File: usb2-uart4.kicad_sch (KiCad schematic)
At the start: 24 parts, among them U1 CH344Q, U13 TPNUP2202W1T2G, Y1 8MHz

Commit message: switch C28-C33 to 0603
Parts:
- C44, C45, C46, C47, C48, C50: footprint Capacitor_SMD:C_0805_2012Metric_Pad1.18x1.45mm_HandSolder -> Capacitor_SMD:C_0603_1608Metric_Pad1.08x0.95mm_HandSolder
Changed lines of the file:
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@@
       (effects (font (size 1.27 1.27)))
     )
-    (property "Footprint" "Capacitor_SMD:C_0805_2012Metric_Pad1.18x1.45mm_HandSolder" (at 126.365 85.09 0)
+    (property "Footprint" "Capacitor_SMD:C_0603_1608Metric_Pad1.08x0.95mm_HandSolder" (at 126.365 85.09 0)
       (effects (font (size 1.27 1.27)) hide)
     )
@@
       (effects (font (size 1.27 1.27)) (justify right))
     )
-    (property "Footprint" "Capacitor_SMD:C_0805_2012Metric_Pad1.18x1.45mm_HandSolder" (at 144.145 119.38 0)
+    (property "Footprint" "Capacitor_SMD:C_0603_1608Metric_Pad1.08x0.95mm_HandSolder" (at 144.145 119.38 0)
       (effects (font (size 1.27 1.27)) hide)
     )
@@
       (effects (font (size 1.27 1.27)))
     )
-    (property "Footprint" "Capacitor_SMD:C_0805_2012Metric_Pad1.18x1.45mm_HandSolder" (at 126.365 81.28 0)
+    (property "Footprint" "Capacitor_SMD:C_0603_1608Metric_Pad1.08x0.95mm_HandSolder" (at 126.365 81.28 0)
       (effects (font (size 1.27 1.27)) hide)
     )
@@
       (effects (font (size 1.27 1.27)))
     )
-    (property "Footprint" "Capacitor_SMD:C_0805_2012Metric_Pad1.18x1.45mm_HandSolder" (at 126.365 88.9 0)
+    (property "Footprint" "Capacitor_SMD:C_0603_1608Metric_Pad1.08x0.95mm_HandSolder" (at 126.365 88.9 0)
       (effects (font (size 1.27 1.27)) hide)
     )
@@
       (effects (font (size 1.27 1.27)))
     )
-    (property "Footprint" "Capacitor_SMD:C_0805_2012Metric_Pad1.18x1.45mm_HandSolder" (at 126.365 92.71 0)
+    (property "Footprint" "Capacitor_SMD:C_0603_1608Metric_Pad1.08x0.95mm_HandSolder" (at 126.365 92.71 0)
       (effects (font (size 1.27 1.27)) hide)
     )
@@
       (effects (font (size 1.27 1.27)) (justify right))
     )
-    (property "Footprint" "Capacitor_SMD:C_0805_2012Metric_Pad1.18x1.45mm_HandSolder" (at 133.985 119.38 0)
-      (effects (font (size 1.27 1.27)) hide)
-    )
+    (property "Footprint" "Capacitor_SMD:C_0603_1608Metric_Pad1.08x0.95mm_HandSolder" (at 133.985 119.38 0)
+      (effects (font (size 1.27 1.27)) hide)
+    )

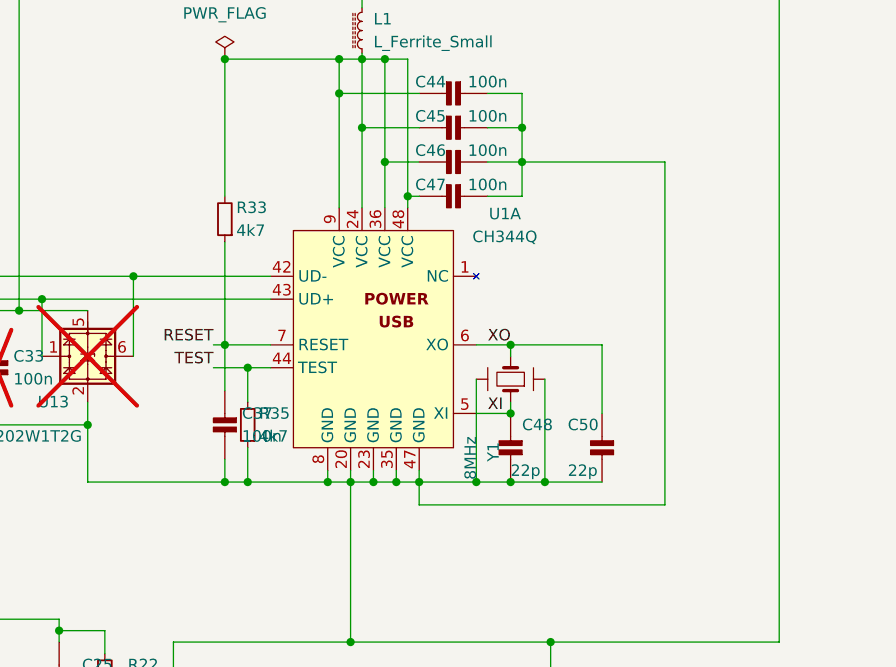
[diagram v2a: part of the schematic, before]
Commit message: Nonfunctional changes to schematic (positions)
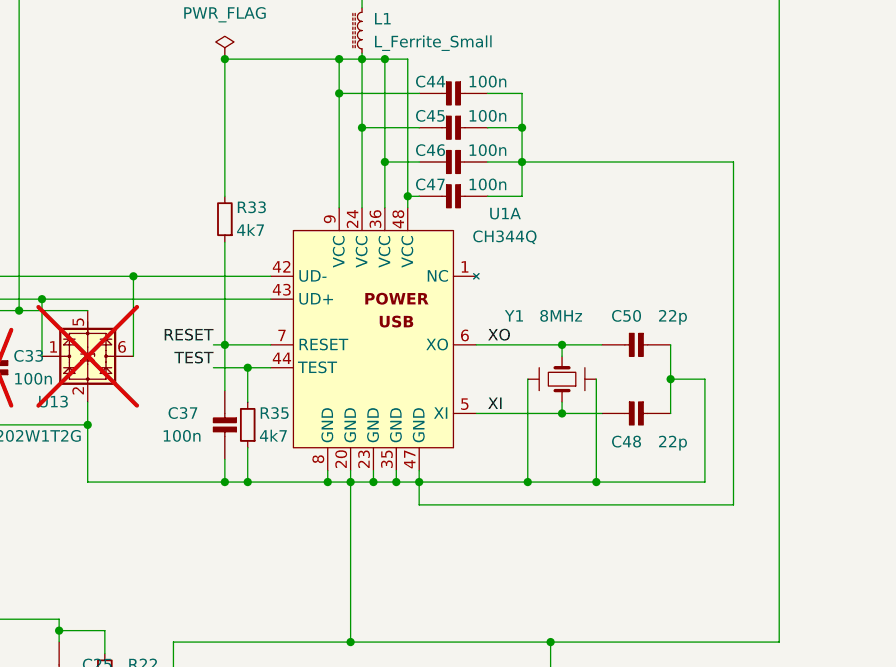
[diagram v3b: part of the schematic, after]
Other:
- moved on the sheet: C48, C50, Y1

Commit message: Fix xtal 7050 footprint warning by creating isouart4 footprint copy
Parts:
- Y1: footprint Crystal:Crystal_SMD_7050-4Pin_7.0x5.0mm -> isouart4:Crystal_SMD_7050-4Pin_7.0x5.0mm
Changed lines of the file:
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@@
       (effects (font (size 1.27 1.27)) (justify right))
     )
-    (property "Footprint" "Crystal:Crystal_SMD_7050-4Pin_7.0x5.0mm" (at 125.73 110.49 0)
+    (property "Footprint" "isouart4:Crystal_SMD_7050-4Pin_7.0x5.0mm" (at 125.73 110.49 0)
       (effects (font (size 1.27 1.27)) hide)
     )

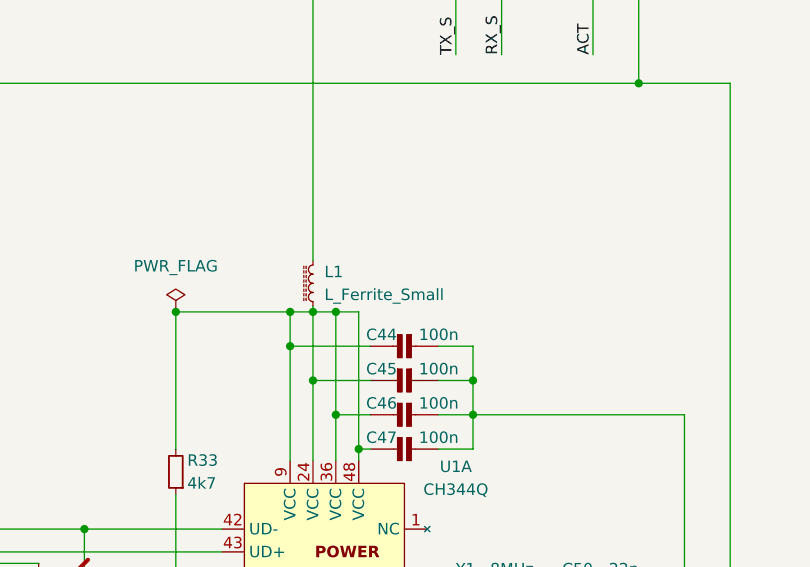
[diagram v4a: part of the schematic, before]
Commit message: Fix FB footprint warning by creating isouart4 footprint copy
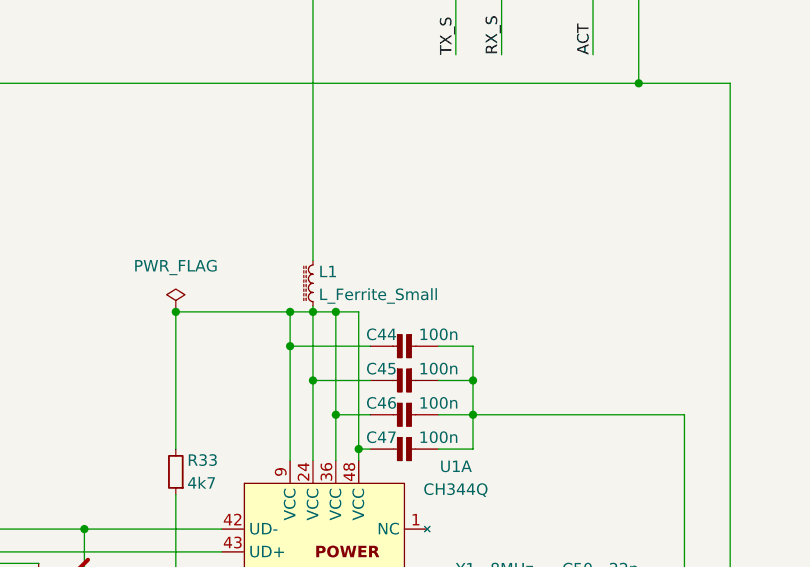
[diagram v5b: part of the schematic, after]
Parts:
- L1: footprint Inductor_SMD:L_TDK_NLV25_2.5x2.0mm -> isouart4:FB_0805_2012Metric; symbol Device:L_Ferrite_Small -> isouart4:L_Ferrite_Small
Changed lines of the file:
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@@
     )
   )
-  (symbol (lib_id "Device:L_Ferrite_Small") (at 117.475 74.295 180) (unit 1)
+  (symbol (lib_id "isouart4:L_Ferrite_Small") (at 117.475 74.295 180) (unit 1)
     (in_bom yes) (on_board yes) (dnp no) (fields_autoplaced)
-    (property "Reference" "L1" (at 118.745 73.025 0)
+    (property "Reference" "L1" (at 118.11 73.025 0)
       (effects (font (size 1.27 1.27)) (justify right))
     )
-    (property "Value" "L_Ferrite_Small" (at 118.745 75.565 0)
+    (property "Value" "L_Ferrite_Small" (at 118.11 75.565 0)
       (effects (font (size 1.27 1.27)) (justify right))
     )
-    (property "Footprint" "Inductor_SMD:L_TDK_NLV25_2.5x2.0mm" (at 117.475 74.295 0)
+    (property "Footprint" "isouart4:FB_0805_2012Metric" (at 117.475 74.295 0)
       (effects (font (size 1.27 1.27)) hide)
     )
